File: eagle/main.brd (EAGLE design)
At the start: 100 x 95 mm, 35 parts, among them IC1 STM32F103, IC2 LM1117, Q1 8MHz

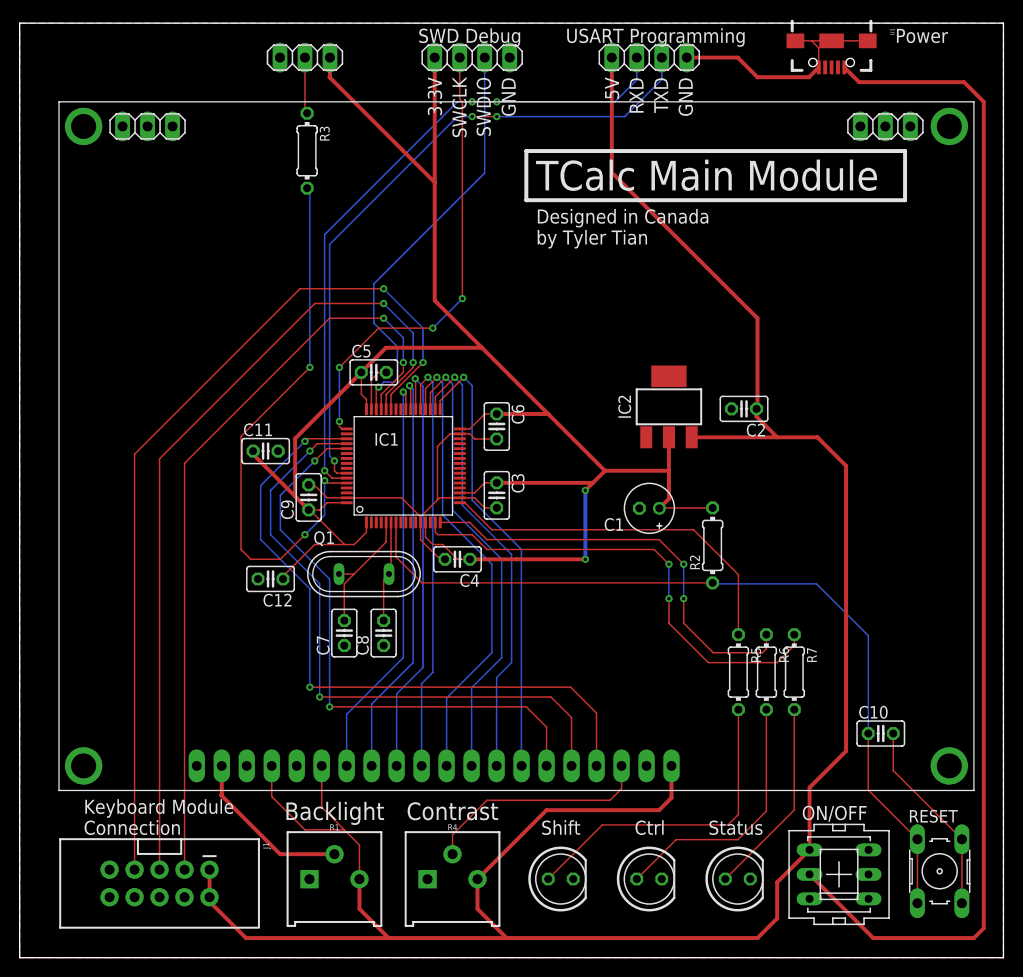
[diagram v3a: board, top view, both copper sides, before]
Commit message: Improve silkscreen
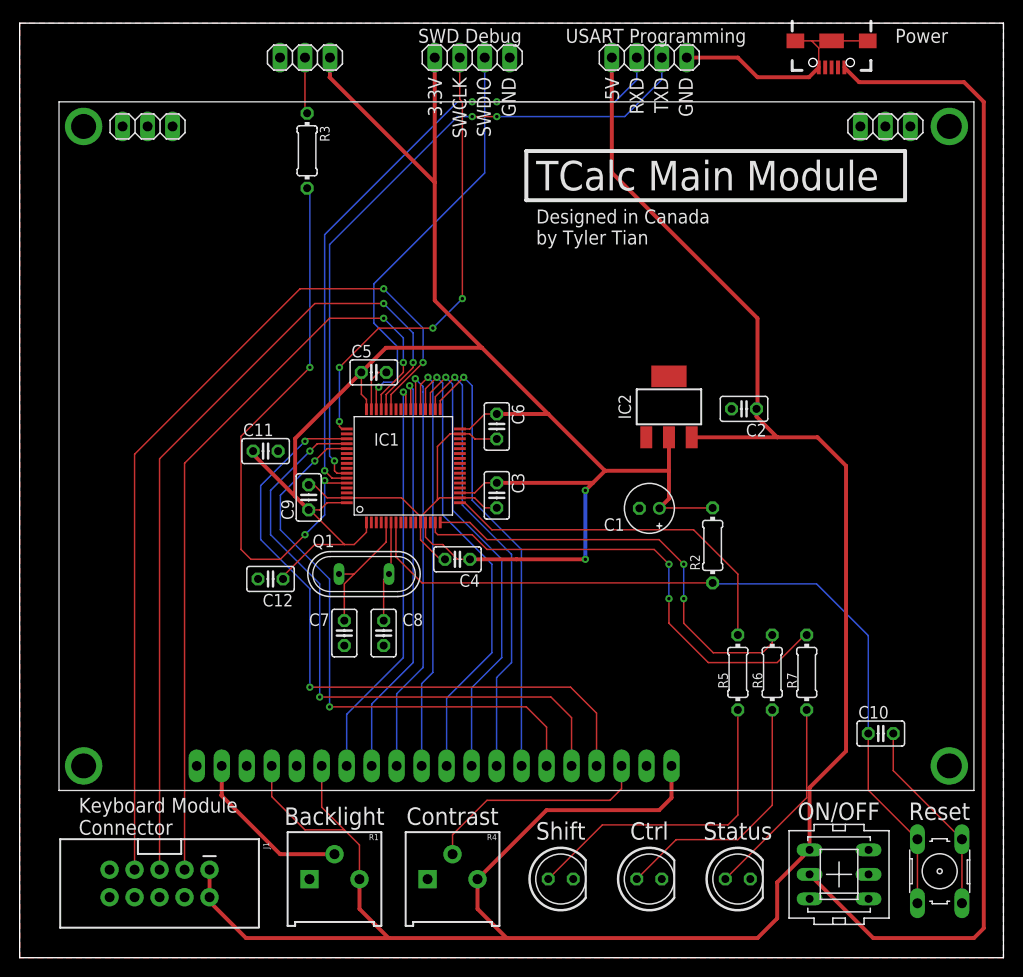
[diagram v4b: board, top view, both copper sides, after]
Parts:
- moved R7 1.26 mm to (80.0, 29.0)
- moved R6 0.60 mm to (76.5, 29.0)
- moved R5 0.07 mm to (73.0, 29.0)
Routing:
- net N$9: track 48.3 -> 48.9 mm
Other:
- board text added: "Keyboard Module Connector"
- board text added: "Reset"
- board text removed: "Keyboard Module Connection"

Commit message: Clean up routes by using a 3.3V fill in the main board
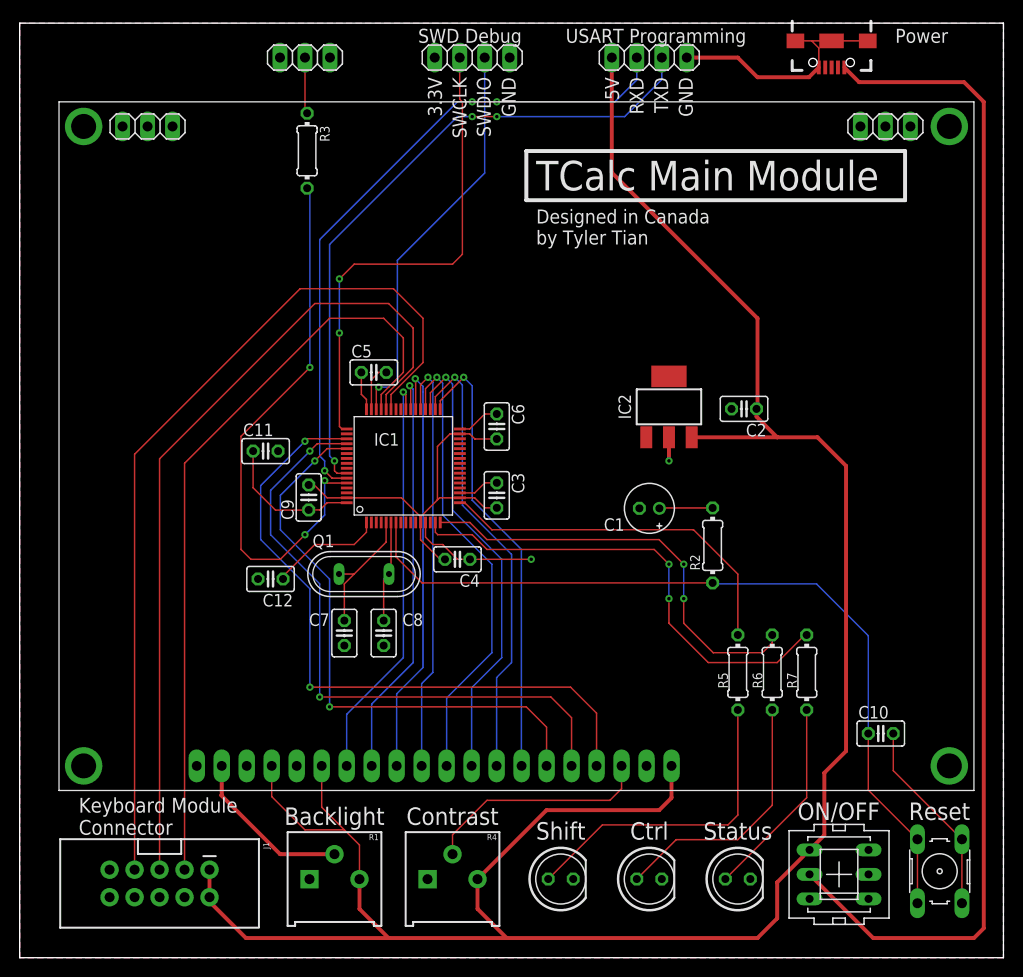
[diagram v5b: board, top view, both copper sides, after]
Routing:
- net 3.3V: track 199.7 -> 59.8 mm
- net SWCLK: track 46.9 -> 49.5 mm, vias 4 -> 2
- net SWDIO: track 42.9 -> 40.9 mm
- net SBDI_DAT: track 89.8 -> 90.4 mm, vias 2 -> 0
- net SBDI_CLK: track 84.2 -> 84.5 mm, vias 2 -> 0
- net SBDI_EN: vias 2 -> 0
- added copper zone on layer 16, net 3.3V

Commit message: Fix error in main schematic
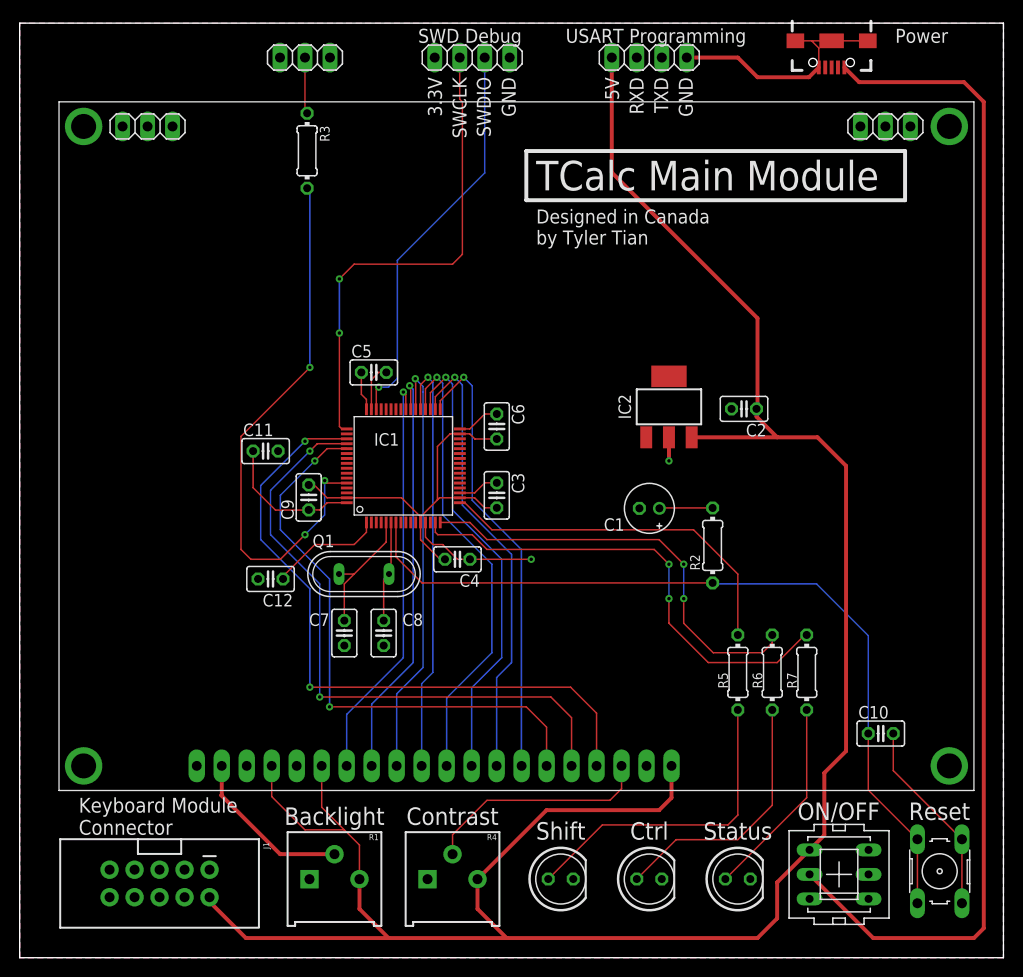
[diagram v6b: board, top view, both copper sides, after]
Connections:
- net RXD: now also IC1.43; no longer IC1.59
- net SBDI_CLK: now also IC1.59; no longer IC1.44
- net SBDI_DAT: now also IC1.58; no longer IC1.43
- net SBDI_EN: now also IC1.61; no longer IC1.45
- net TXD: now also IC1.42; no longer IC1.58
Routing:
- net SBDI_DAT: track 90.4 -> 0.00 mm
- net SBDI_CLK: track 84.5 -> 0.00 mm
- net SBDI_EN: track 78.7 -> 0.00 mm
- net TXD: track 67.5 -> 0.00 mm, vias 3 -> 0
- net RXD: track 67.5 -> 0.00 mm, vias 3 -> 0
- net VCC: track 240.6 -> 237.3 mm
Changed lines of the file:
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@@
 <contactref element="R4" pad="1"/>
 <contactref element="GLCD2" pad="2"/>
-<contactref element="J1" pad="9"/>
-<contactref element="J1" pad="10"/>
 <contactref element="GLCD2" pad="20"/>
 <contactref element="R1" pad="1"/>
@@
 <wire x1="40.75" y1="44.25" x2="40.75" y2="44.8232875" width="0.1524" layer="1"/>
 <wire x1="40.75" y1="44.8232875" x2="42.46335625" y2="46.53664375" width="0.1524" layer="1"/>
+<contactref element="J1" pad="9"/>
+<contactref element="J1" pad="10"/>
+<wire x1="49.81" y1="91.5" x2="67.81" y2="91.5" width="0" layer="19" extent="1-1"/>
+<wire x1="26.46" y1="91.5" x2="49.81" y2="91.5" width="0" layer="19" extent="1-1"/>
+<wire x1="36.5" y1="59.5" x2="26.46" y2="91.5" width="0" layer="19" extent="1-1"/>
+<wire x1="42.46335625" y1="51.96335625" x2="35.75" y2="55.75" width="0" layer="19" extent="1-1"/>
+<wire x1="26.27" y1="51.5" x2="29.38" y2="48.06" width="0" layer="19" extent="1-1"/>
+<wire x1="37" y1="31.73" x2="42.73" y2="40.5" width="0" layer="19" extent="1-1"/>
+<wire x1="33" y1="31.73" x2="37" y2="31.73" width="0" layer="19" extent="1-1"/>
+<wire x1="24.23" y1="38.5" x2="31.25" y2="46.75" width="0" layer="19" extent="1-1"/>
+<wire x1="62.994" y1="45.68" x2="48.5" y2="45.73" width="0" layer="19" extent="1-1"/>
+<wire x1="63.689" y1="52.901" x2="62.994" y2="45.68" width="0" layer="19" extent="1-1"/>
+<wire x1="72.36" y1="55.79" x2="63.689" y2="52.901" width="0" layer="19" extent="1-1"/>
+<wire x1="18" y1="19.5" x2="33" y2="31.73" width="0" layer="19" extent="1-1"/>
+<wire x1="9.14" y1="8.947" x2="18" y2="19.5" width="0" layer="19" extent="1-1"/>
+<wire x1="9.14" y1="6.153" x2="9.14" y2="8.947" width="0" layer="19" extent="1-1"/>
+<wire x1="29.46" y1="7.985" x2="18" y2="19.5" width="0" layer="19" extent="1-1"/>
+<wire x1="41.46" y1="7.985" x2="29.46" y2="7.985" width="0" layer="19" extent="1-1"/>
+<wire x1="56.27" y1="8" x2="41.46" y2="7.985" width="0" layer="19" extent="1-1"/>
+<wire x1="65.27" y1="8" x2="56.27" y2="8" width="0" layer="19" extent="1-1"/>
+<wire x1="74.27" y1="8" x2="65.27" y2="8" width="0" layer="19" extent="1-1"/>
+<wire x1="63.72" y1="19.5" x2="65.27" y2="8" width="0" layer="19" extent="1-1"/>
+<wire x1="88.8" y1="19.0218" x2="74.27" y2="8" width="0" layer="19" extent="1-1"/>
 </signal>
 <signal name="VCC">
@@
 <contactref element="R4" pad="3"/>
 <contactref element="GLCD2" pad="1"/>
-<contactref element="J1" pad="1"/>
-<contactref element="J1" pad="2"/>
 <contactref element="GLCD2" pad="15"/>
 <contactref element="R1" pad="3"/>
@@
 <wire x1="77" y1="4" x2="75" y2="2" width="0.4" layer="1"/>
 <wire x1="23" y1="2" x2="19.3" y2="5.7" width="0.4" layer="1"/>
-<wire x1="19.3" y1="5.7" x2="19.3" y2="6.153" width="0.4" layer="1"/>
 <wire x1="75" y1="2" x2="49.5" y2="2" width="0.4" layer="1"/>
 <wire x1="49.5" y1="2" x2="37.5" y2="2" width="0.4" layer="1"/>
 <wire x1="37.5" y1="2" x2="23" y2="2" width="0.4" layer="1"/>
-<wire x1="19.3" y1="6.153" x2="19.3" y2="8.947" width="0.4" layer="1"/>
 <wire x1="60.19" y1="91.5" x2="60.19" y2="79.81" width="0.4" layer="1"/>
 <wire x1="60.19" y1="79.81" x2="75" y2="65" width="0.4" layer="1"/>
@@
 <wire x1="30.7" y1="19.5" x2="30.7" y2="15.3" width="0.1524" layer="1"/>
 <wire x1="33" y1="13" x2="30.7" y2="15.3" width="0.1524" layer="1"/>
-</signal>
-<signal name="SBDI_EN">
-<contactref element="J1" pad="3"/>
-<contactref element="IC1" pad="45"/>
-<wire x1="16.76" y1="50.26" x2="31.5" y2="65" width="0.1524" layer="1"/>
-<wire x1="16.76" y1="50.26" x2="16.76" y2="8.947" width="0.1524" layer="1"/>
-<wire x1="36.75" y1="55.75" x2="36.75" y2="57.25" width="0.1524" layer="1"/>
-<wire x1="39" y1="59.5" x2="36.75" y2="57.25" width="0.1524" layer="1"/>
-<wire x1="31.5" y1="65" x2="37" y2="65" width="0.1524" layer="1"/>
-<wire x1="37" y1="65" x2="39" y2="63" width="0.1524" layer="1"/>
-<wire x1="39" y1="63" x2="39" y2="59.5" width="0.1524" layer="1"/>
-</signal>
-<signal name="SBDI_CLK">
-<contactref element="J1" pad="5"/>
-<contactref element="IC1" pad="44"/>
-<wire x1="14.22" y1="8.947" x2="14.22" y2="50.72" width="0.1524" layer="1"/>
-<wire x1="14.22" y1="50.72" x2="30" y2="66.5" width="0.1524" layer="1"/>
-<wire x1="37.25" y1="55.75" x2="37.25" y2="57.25" width="0.1524" layer="1"/>
-<wire x1="40" y1="60" x2="37.25" y2="57.25" width="0.1524" layer="1"/>
-<wire x1="37.5" y1="66.5" x2="40" y2="64" width="0.1524" layer="1"/>
-<wire x1="30" y1="66.5" x2="37.5" y2="66.5" width="0.1524" layer="1"/>
-<wire x1="40" y1="64" x2="40" y2="60" width="0.1524" layer="1"/>
-</signal>
-<signal name="SBDI_DAT">
-<contactref element="J1" pad="7"/>
-<contactref element="IC1" pad="43"/>
-<wire x1="11.68" y1="51.18" x2="11.68" y2="8.947" width="0.1524" layer="1"/>
-<wire x1="11.68" y1="51.18" x2="28.5" y2="68" width="0.1524" layer="1"/>
-<wire x1="37.75" y1="55.75" x2="37.75" y2="57.25" width="0.1524" layer="1"/>
-<wire x1="41" y1="60.5" x2="37.75" y2="57.25" width="0.1524" layer="1"/>
-<wire x1="38" y1="68" x2="41" y2="65" width="0.1524" layer="1"/>
-<wire x1="41" y1="65" x2="41" y2="60.5" width="0.1524" layer="1"/>
-<wire x1="28.5" y1="68" x2="38" y2="68" width="0.1524" layer="1"/>
-</signal>
-<signal name="TXD">
-<contactref element="IC1" pad="58"/>
-<contactref element="JP3" pad="3"/>
-<wire x1="33.25" y1="49.25" x2="32.25" y2="49.25" width="0.1524" layer="1"/>
-<wire x1="32.25" y1="49.25" x2="32" y2="49.5" width="0.1524" layer="1"/>
-<wire x1="32" y1="49.5" x2="32" y2="50.5" width="0.1524" layer="1"/>
-<via x="32" y="50.5" extent="1-16" drill="0.35"/>
-<wire x1="32" y1="50.5" x2="31.5" y2="51" width="0.1524" layer="16"/>
-<wire x1="31.5" y1="51" x2="31.5" y2="72.5" width="0.1524" layer="16"/>
-<wire x1="31.5" y1="72.5" x2="44.5" y2="85.5" width="0.1524" layer="16"/>
-<wire x1="44.5" y1="85.5" x2="46" y2="85.5" width="0.1524" layer="16"/>
-<via x="46" y="85.5" extent="1-16" drill="0.35"/>
-<wire x1="46" y1="85.5" x2="48.5" y2="85.5" width="0.1524" layer="1"/>
-<via x="48.5" y="85.5" extent="1-16" drill="0.35"/>
-<wire x1="48.5" y1="85.5" x2="61.5" y2="85.5" width="0.1524" layer="16"/>
-<wire x1="65.27" y1="89.27" x2="65.27" y2="91.5" width="0.1524" layer="16"/>
-<wire x1="61.5" y1="85.5" x2="65.27" y2="89.27" width="0.1524" layer="16"/>
-</signal>
-<signal name="RXD">
-<contactref element="IC1" pad="59"/>
-<contactref element="JP3" pad="2"/>
-<wire x1="33.25" y1="48.75" x2="31.75" y2="48.75" width="0.1524" layer="1"/>
-<wire x1="31.75" y1="48.75" x2="31" y2="49.5" width="0.1524" layer="1"/>
-<via x="31" y="49.5" extent="1-16" drill="0.35"/>
-<wire x1="30.5" y1="73" x2="30.5" y2="51" width="0.1524" layer="16"/>
-<wire x1="31" y1="49.5" x2="31" y2="50.5" width="0.1524" layer="16"/>
-<wire x1="31" y1="50.5" x2="30.5" y2="51" width="0.1524" layer="16"/>
-<wire x1="44.5" y1="87" x2="46" y2="87" width="0.1524" layer="16"/>
-<via x="46" y="87" extent="1-16" drill="0.35"/>
-<wire x1="46" y1="87" x2="48.5" y2="87" width="0.1524" layer="1"/>
-<via x="48.5" y="87" extent="1-16" drill="0.35"/>
-<wire x1="62.73" y1="89.23" x2="62.73" y2="91.5" width="0.1524" layer="16"/>
-<wire x1="30.5" y1="73" x2="44.5" y2="87" width="0.1524" layer="16"/>
-<wire x1="48.5" y1="87" x2="60.5" y2="87" width="0.1524" layer="16"/>
-<wire x1="60.5" y1="87" x2="62.73" y2="89.23" width="0.1524" layer="16"/>
+<contactref element="J1" pad="1"/>
+<contactref element="J1" pad="2"/>
+<wire x1="19.3" y1="6.153" x2="19.3" y2="8.947" width="0" layer="19" extent="1-1"/>
+<wire x1="19.3" y1="5.7" x2="19.3" y2="6.153" width="0" layer="19" extent="1-1"/>
 </signal>
 <signal name="N$5">
@@
 <wire x1="86.7628" y1="2" x2="80.2928" y2="8.47" width="0.4" layer="1"/>
 </signal>
+<signal name="TXD">
+<contactref element="IC1" pad="42"/>
+<contactref element="JP3" pad="3"/>
+<wire x1="38.25" y1="55.75" x2="65.27" y2="91.5" width="0" layer="19" extent="1-1"/>
+</signal>
+<signal name="RXD">
+<contactref element="IC1" pad="43"/>
+<contactref element="JP3" pad="2"/>
+<wire x1="37.75" y1="55.75" x2="62.73" y2="91.5" width="0" layer="19" extent="1-1"/>
+</signal>
+<signal name="SBDI_EN">
+<contactref element="J1" pad="3"/>
+<contactref element="IC1" pad="61"/>
+<wire x1="16.76" y1="8.947" x2="33.25" y2="47.75" width="0" layer="19" extent="1-1"/>
+</signal>
+<signal name="SBDI_CLK">
+<contactref element="IC1" pad="59"/>
+<contactref element="J1" pad="5"/>
+<wire x1="14.22" y1="8.947" x2="33.25" y2="48.75" width="0" layer="19" extent="1-1"/>
+</signal>
+<signal name="SBDI_DAT">
+<contactref element="J1" pad="7"/>
+<contactref element="IC1" pad="58"/>
+<wire x1="11.68" y1="8.947" x2="33.25" y2="49.25" width="0" layer="19" extent="1-1"/>
+</signal>
 </signals>

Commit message: Reroute main board
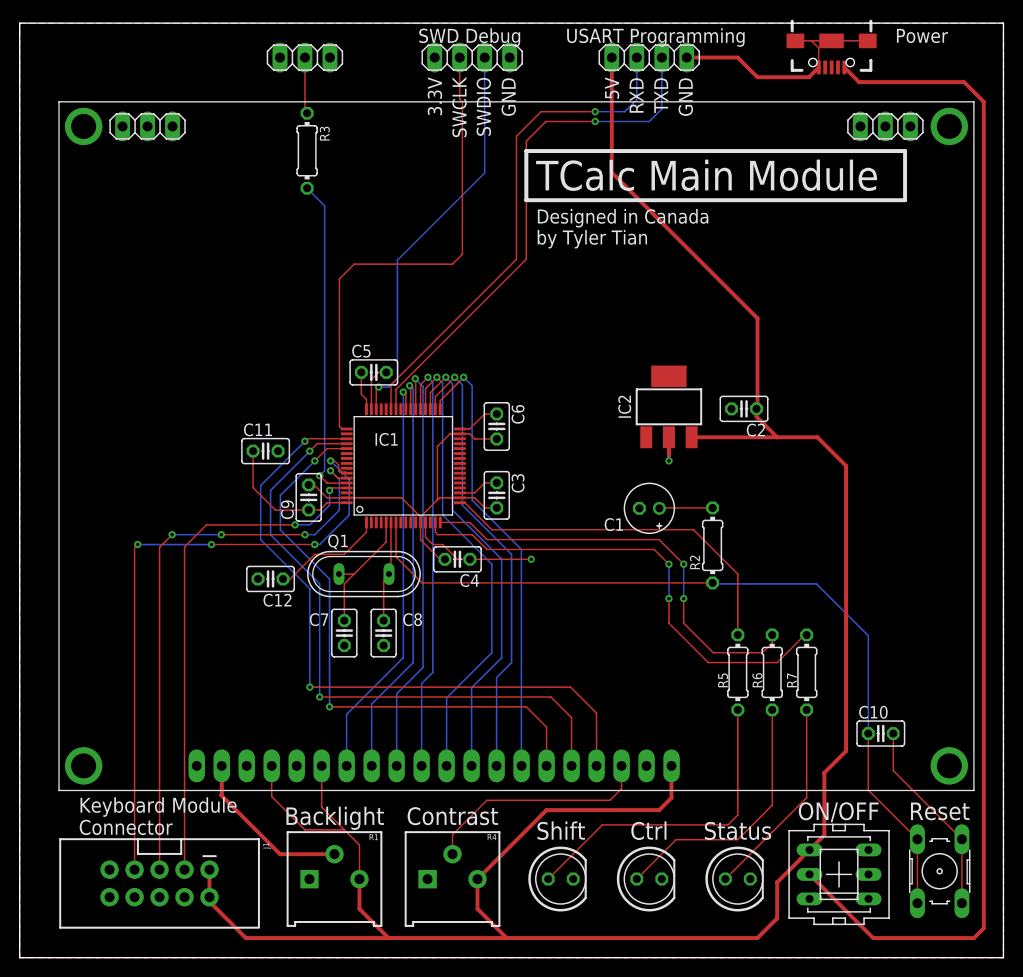
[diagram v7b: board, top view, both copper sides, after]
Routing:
- net SBDI_DAT: track 0.00 -> 64.7 mm, vias 0 -> 4
- net SBDI_CLK: track 0.00 -> 58.9 mm, vias 0 -> 4
- net TXD: track 0.00 -> 53.1 mm, vias 0 -> 1
- net SBDI_EN: track 0.00 -> 52.7 mm, vias 0 -> 2
- net RXD: track 0.00 -> 51.1 mm, vias 0 -> 1
- net N$10: track 56.4 -> 33.2 mm, vias 3 -> 1
- net VCC: track 237.3 -> 240.6 mm
- net SWCLK: vias 2 -> 0
